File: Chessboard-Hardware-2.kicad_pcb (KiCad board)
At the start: 2 copper layers, 200 x 200 mm, 5 parts, among them J1 Raspberry_Pi_0

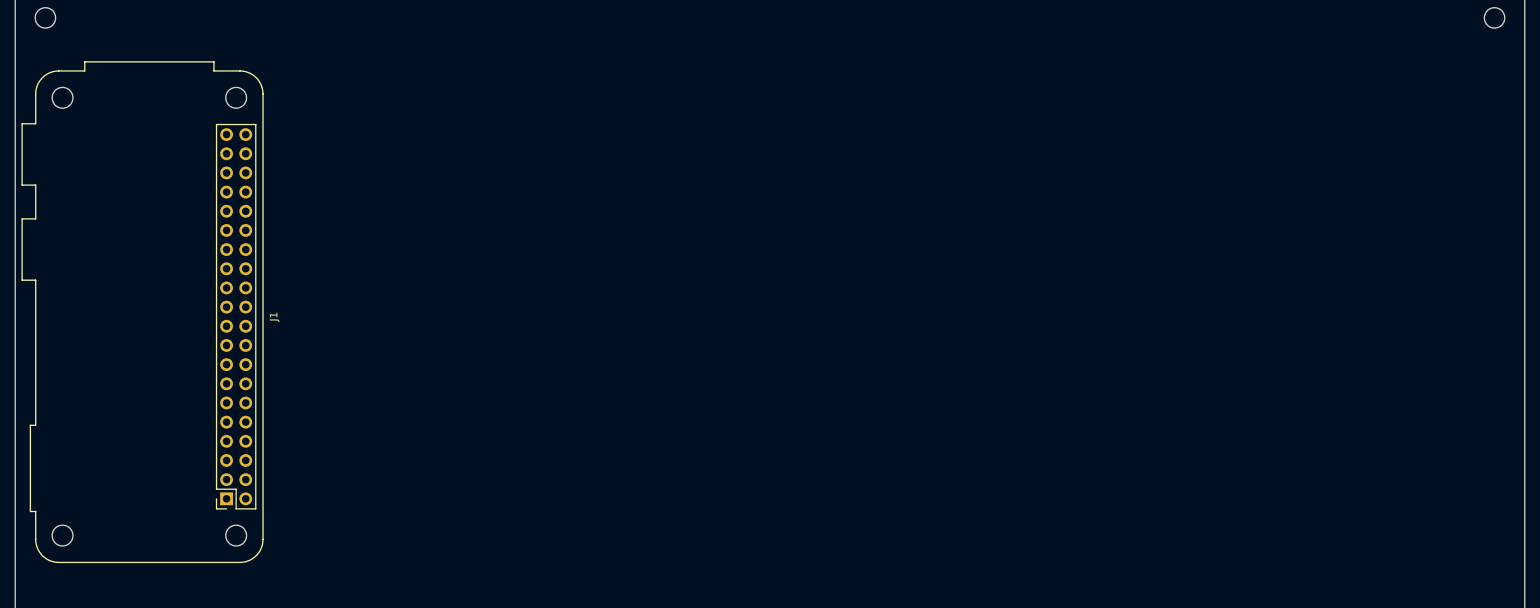
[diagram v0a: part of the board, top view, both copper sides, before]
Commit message: Add JST-XH connector and schematic
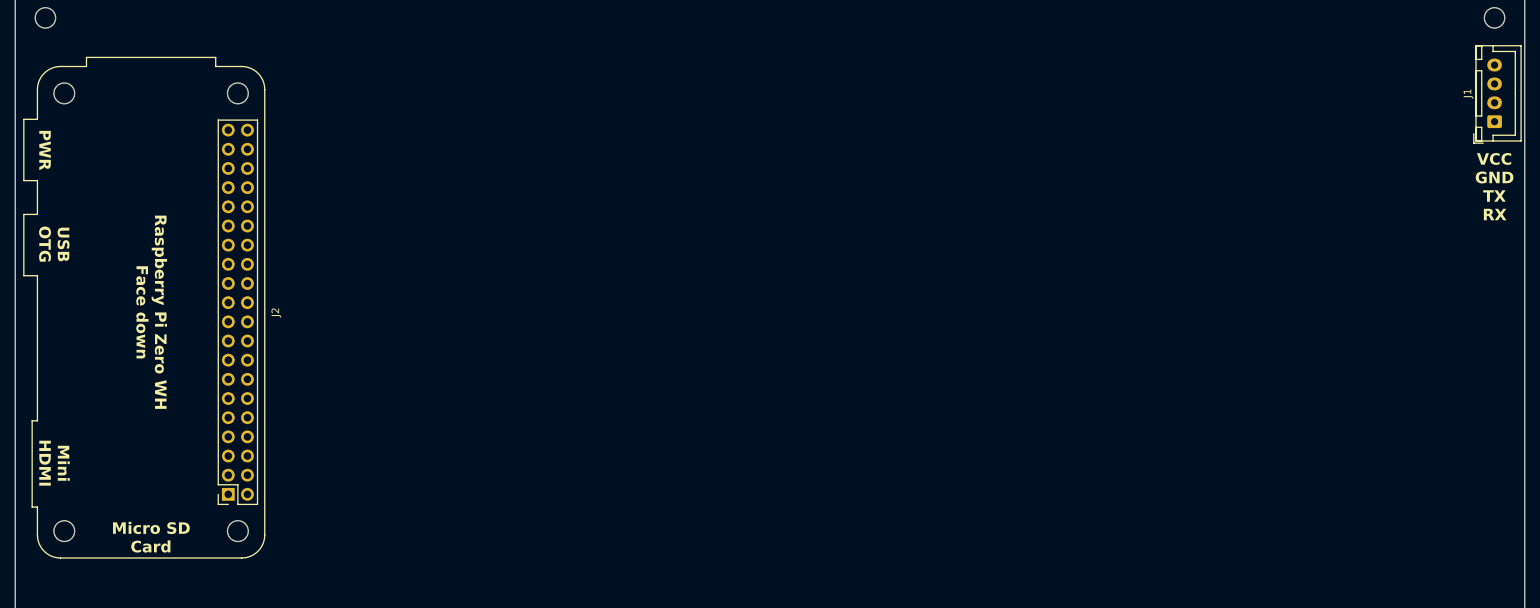
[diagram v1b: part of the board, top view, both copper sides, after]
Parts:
- added J2: Raspberry_Pi_0, Project Library:Raspberry_Pi_Zero_Socketed_THT_FaceDown_MountingHoles, F.Cu at (68.0, 93.0)
- J1: value Raspberry_Pi_0 -> Conn_01x04_Pin; footprint Project Library:Raspberry_Pi_Zero_Socketed_THT_FaceDown_MountingHoles -> Connector_JST:JST_XH_B4B-XH-A_1x04_P2.50mm_Vertical
- moved J1 180.1 mm to (246.0, 67.8), turned to 90 degrees
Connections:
- J1 pad 1: unconnected-(J1-3V3-Pad1) -> /RX
- J1 pad 2: unconnected-(J1-5V-Pad2) -> /TX
- J1 pad 3: unconnected-(J1-SDA/GPIO2-Pad3) -> GND
- J1 pad 4: 5V -> +5V
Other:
- board text added: "Micro SD Card"
- board text added: "Mini HDMI"
- board text added: "PWR"
- board text added: "Raspberry Pi Zero WH Face down"
- board text added: "USB OTG"
- board text added: "VCC GND TX RX"

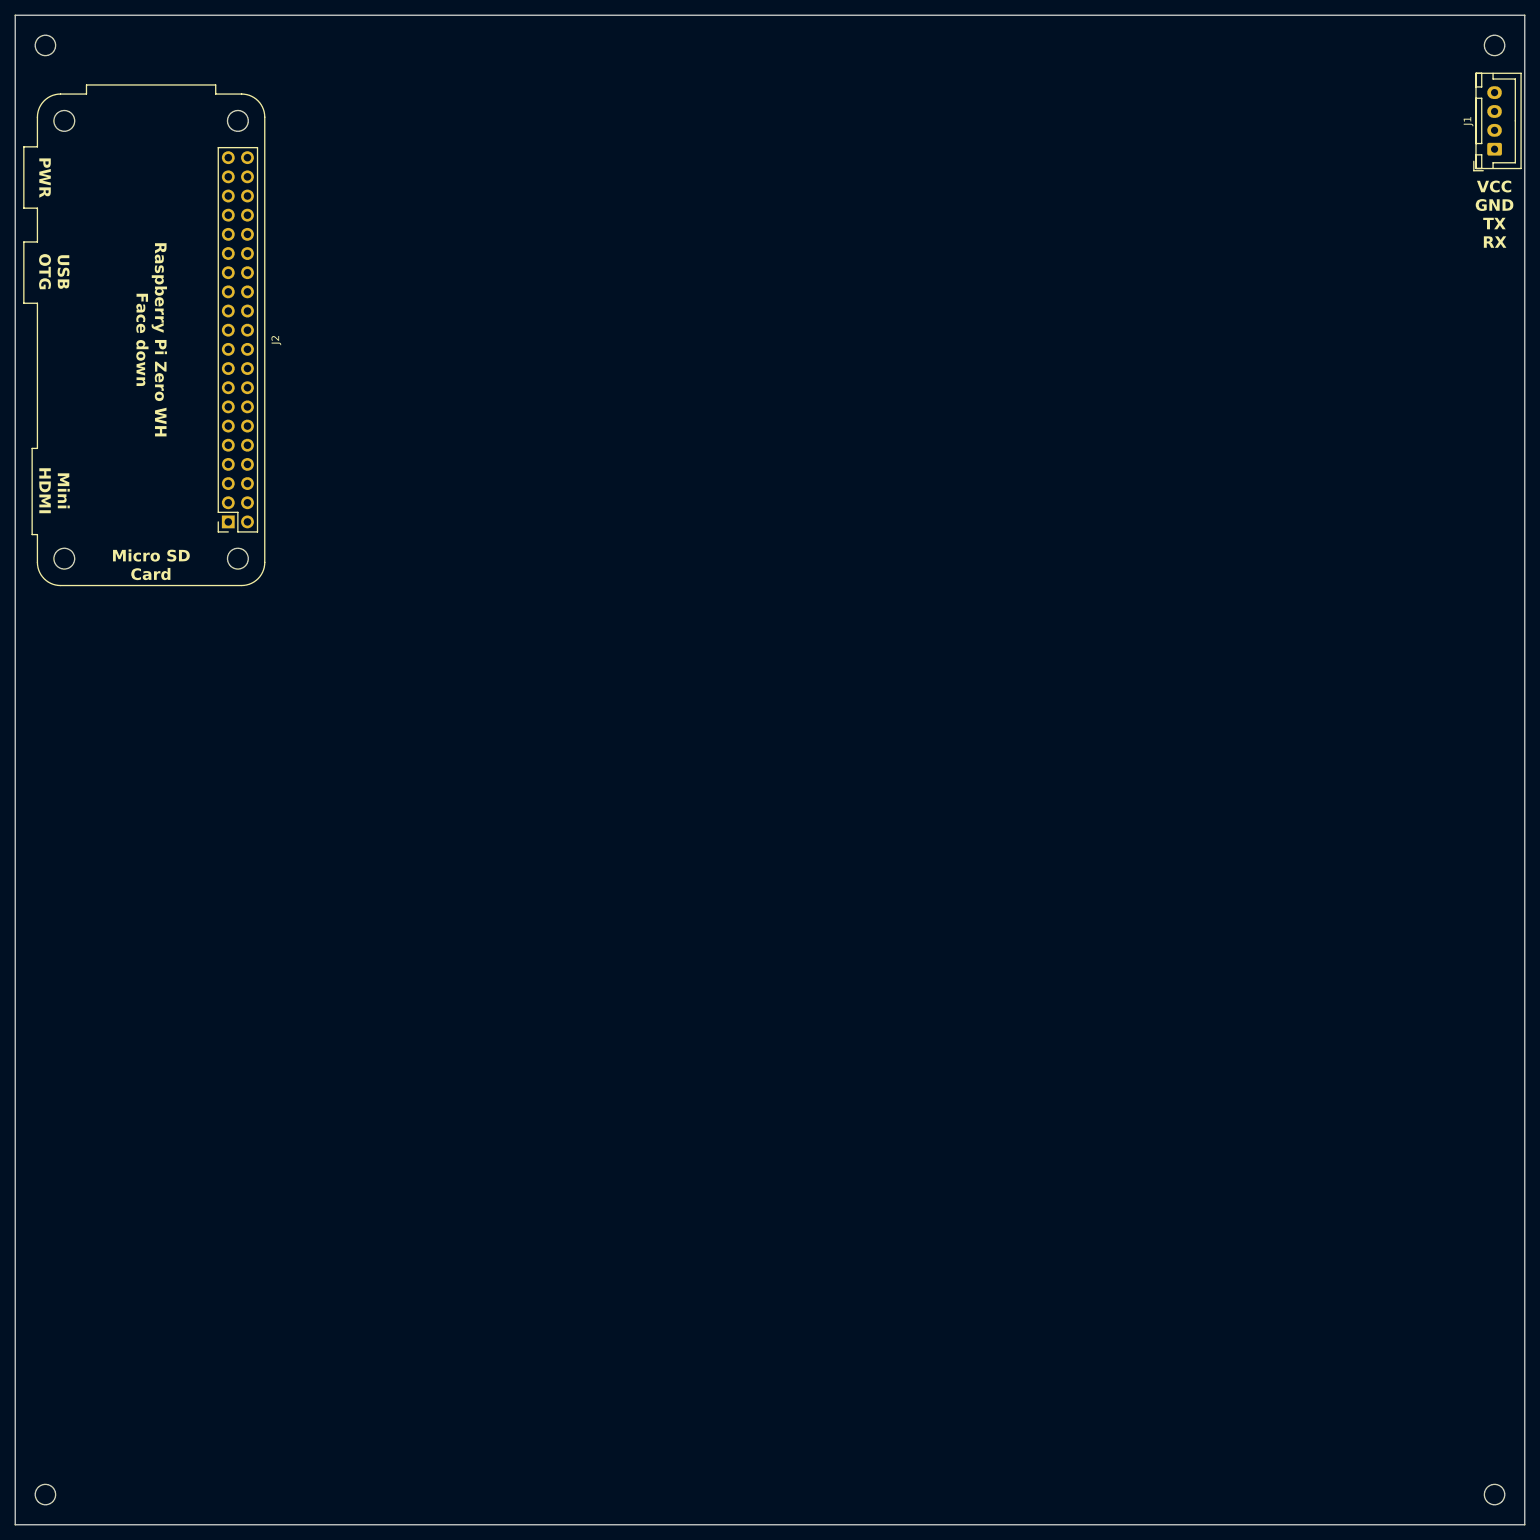
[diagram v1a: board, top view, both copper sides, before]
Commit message: Schematic and PCB for wiring up Pi to Nano
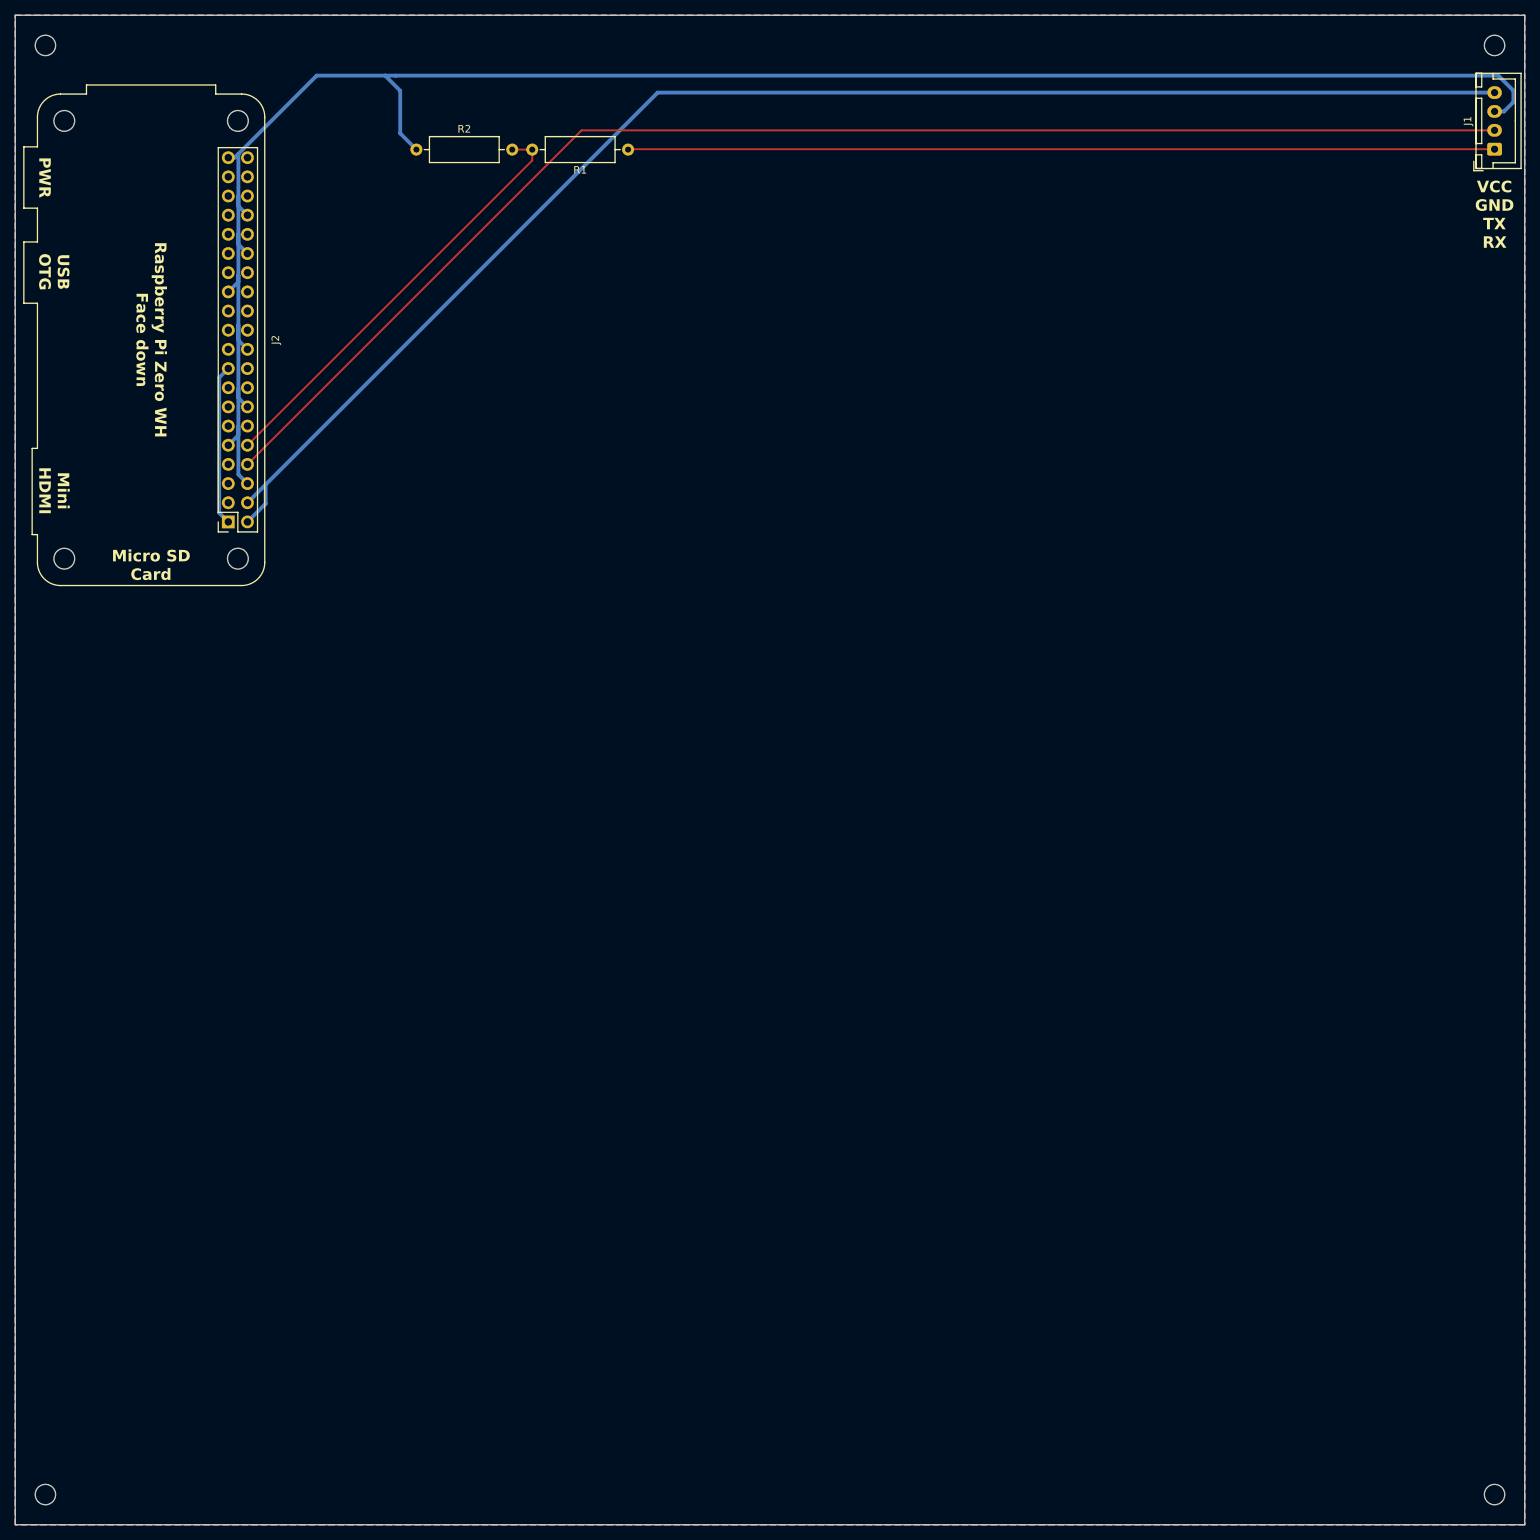
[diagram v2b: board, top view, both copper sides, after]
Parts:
- added R1: 5.1K, Resistor_THT:R_Axial_DIN0309_L9.0mm_D3.2mm_P12.70mm_Horizontal, F.Cu at (131.2, 67.8)
- added R2: 5.1K, Resistor_THT:R_Axial_DIN0309_L9.0mm_D3.2mm_P12.70mm_Horizontal, F.Cu at (103.2, 67.8)
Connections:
- J1 pad 1: /RX -> Net-(J1-Pin_1)
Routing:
- net GND: track 0.00 -> 254.3 mm
- net +5V: track 0.00 -> 193.7 mm
- net /TX: track 0.00 -> 183.6 mm
- net Net-(J1-Pin_1): track 0.00 -> 114.8 mm
- net /RX: track 0.00 -> 57.4 mm
- net +3.3V: track 0.00 -> 21.3 mm
- added copper zone on B.Cu, net GND
- added copper zone on F.Cu, net GND

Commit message: Add test points
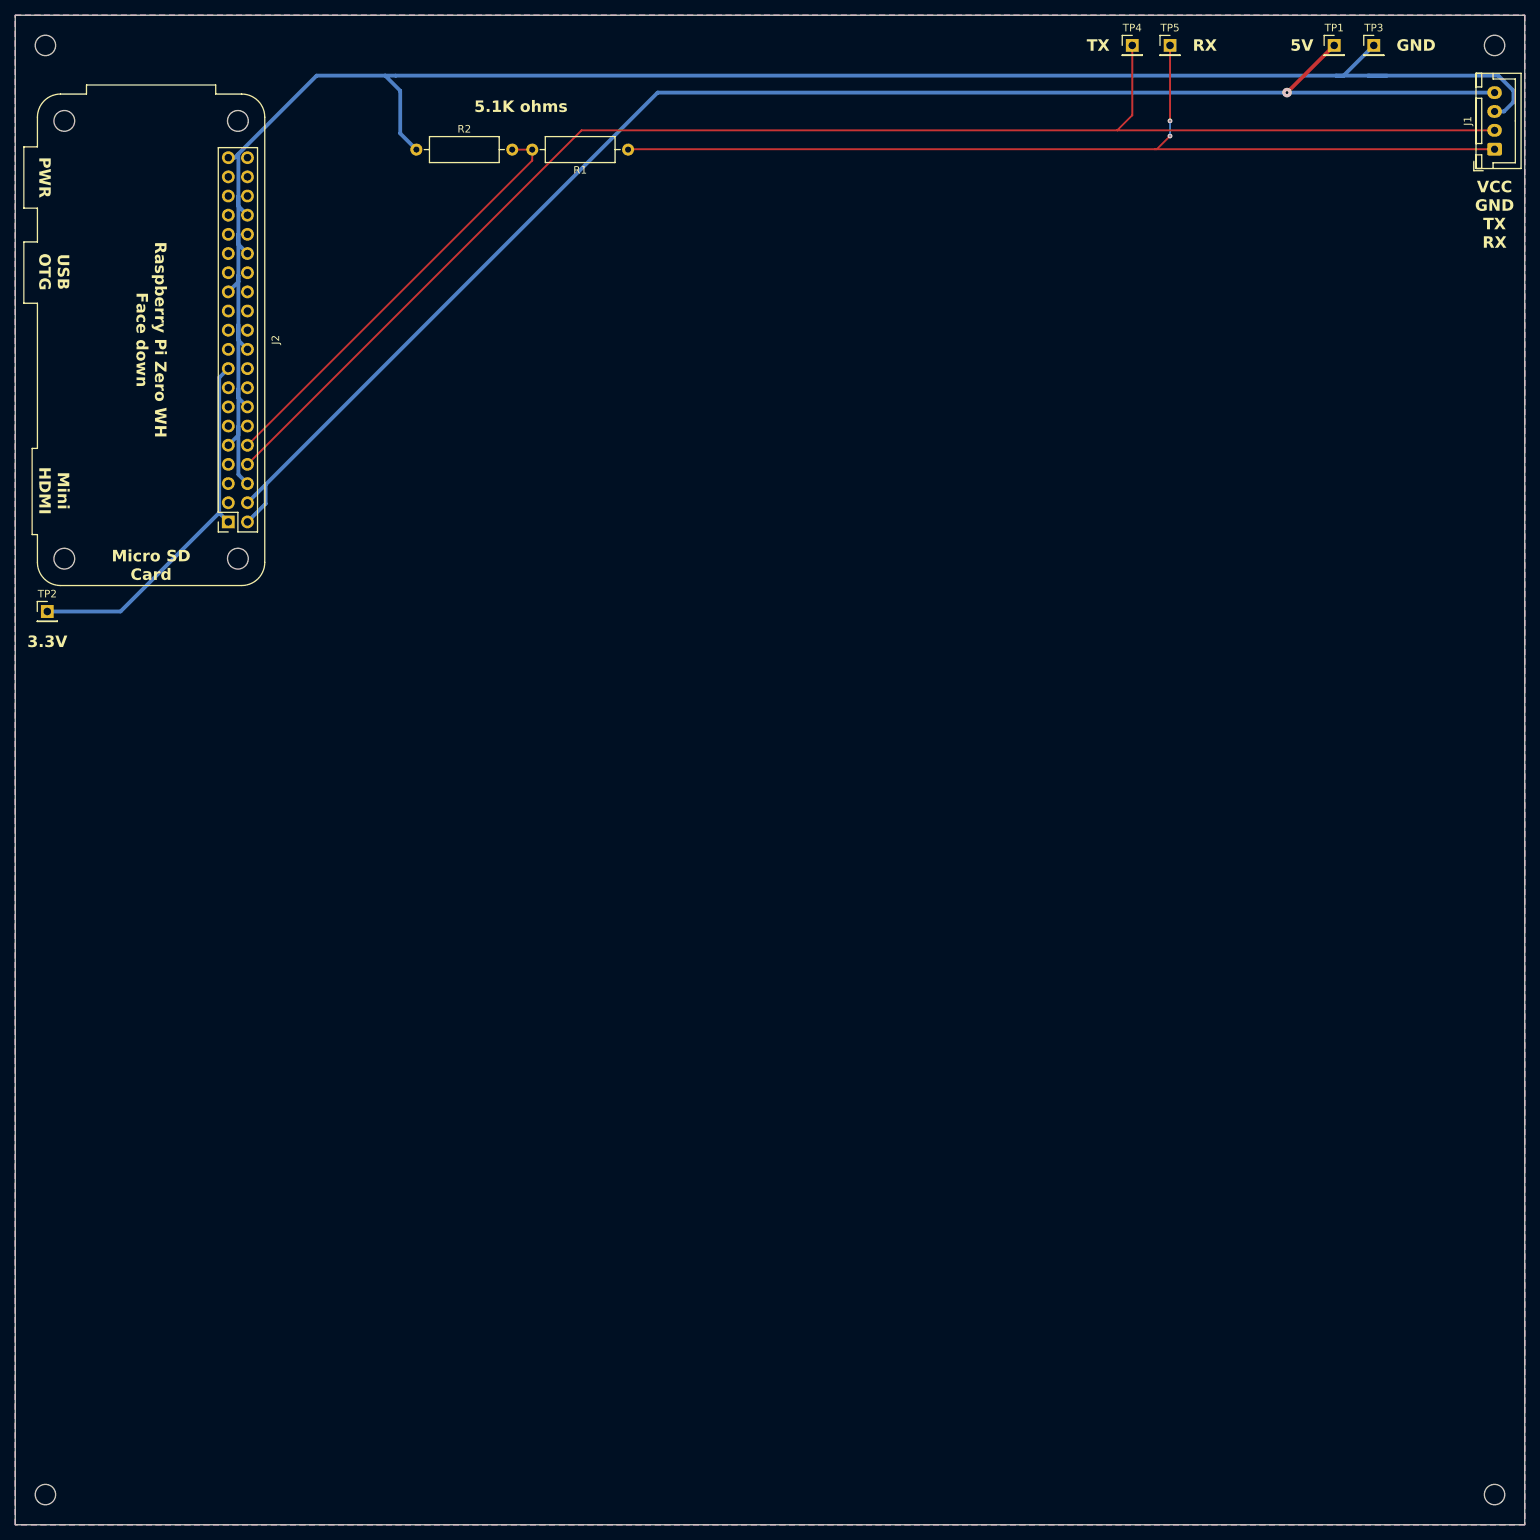
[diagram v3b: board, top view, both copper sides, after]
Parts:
- added TP1: TestPoint, Connector_PinHeader_2.54mm:PinHeader_1x01_P2.54mm_Vertical, F.Cu at (224.8, 54.0)
- added TP2: TestPoint, Connector_PinHeader_2.54mm:PinHeader_1x01_P2.54mm_Vertical, F.Cu at (54.2, 129.0)
- added TP3: TestPoint, Connector_PinHeader_2.54mm:PinHeader_1x01_P2.54mm_Vertical, F.Cu at (230.0, 54.0)
- added TP4: TestPoint, Connector_PinHeader_2.54mm:PinHeader_1x01_P2.54mm_Vertical, F.Cu at (198.0, 54.0)
- added TP5: TestPoint, Connector_PinHeader_2.54mm:PinHeader_1x01_P2.54mm_Vertical, F.Cu at (203.0, 54.0)
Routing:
- net +3.3V: track 21.3 -> 49.5 mm
- net Net-(J1-Pin_1): track 114.8 -> 129.5 mm, vias 0 -> 2
- net /TX: track 183.6 -> 195.6 mm
- net GND: track 254.3 -> 263.4 mm
- net +5V: track 193.7 -> 202.5 mm, vias 0 -> 1
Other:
- board text added: "3.3V"
- board text added: "5.1K ohms"
- board text added: "5V"
- board text added: "GND"
- board text added: "RX"
- board text added: "TX"
